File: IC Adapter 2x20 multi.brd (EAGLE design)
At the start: 74 x 56 mm, 12 parts, among them IC2 LTC6804IG-1#PBF, IC3 LTC6804IG-1#PBF, IC4 LTC6804IG-1#PBF

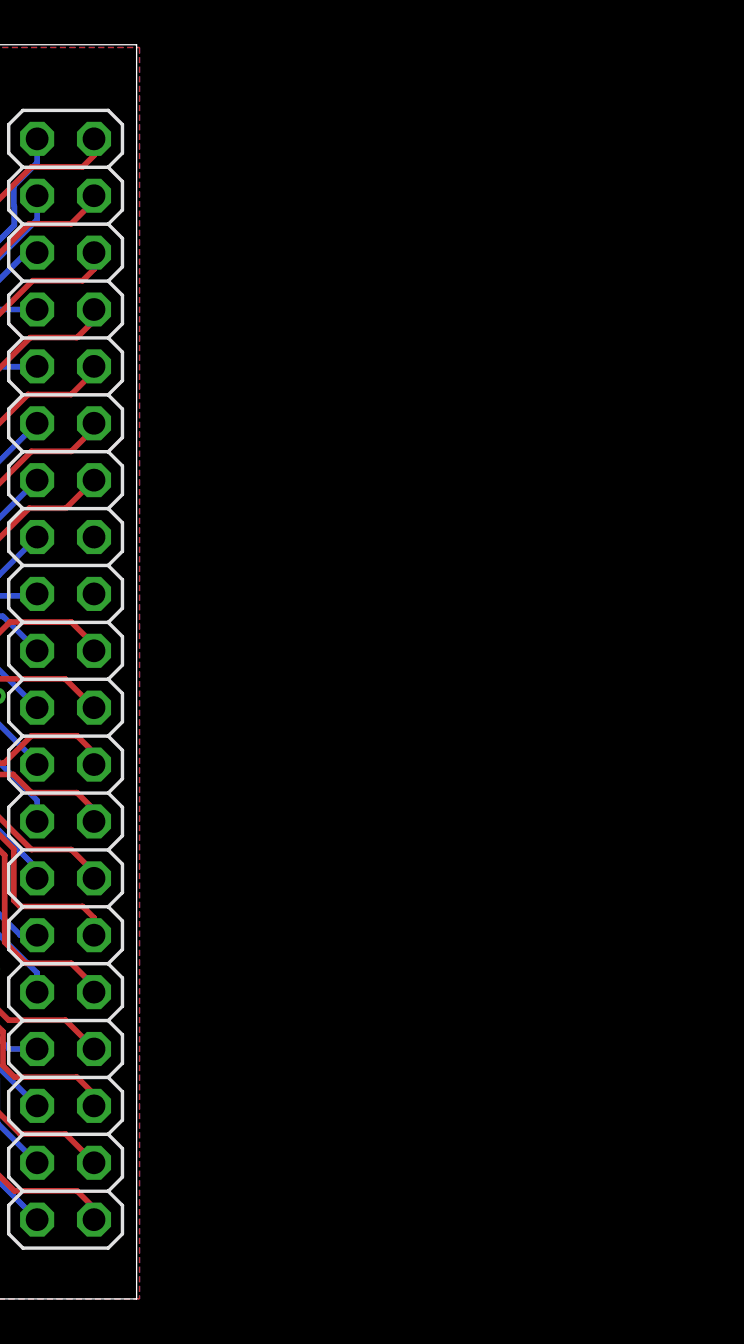
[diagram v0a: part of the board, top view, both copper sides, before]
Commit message: multi made to 4x boards
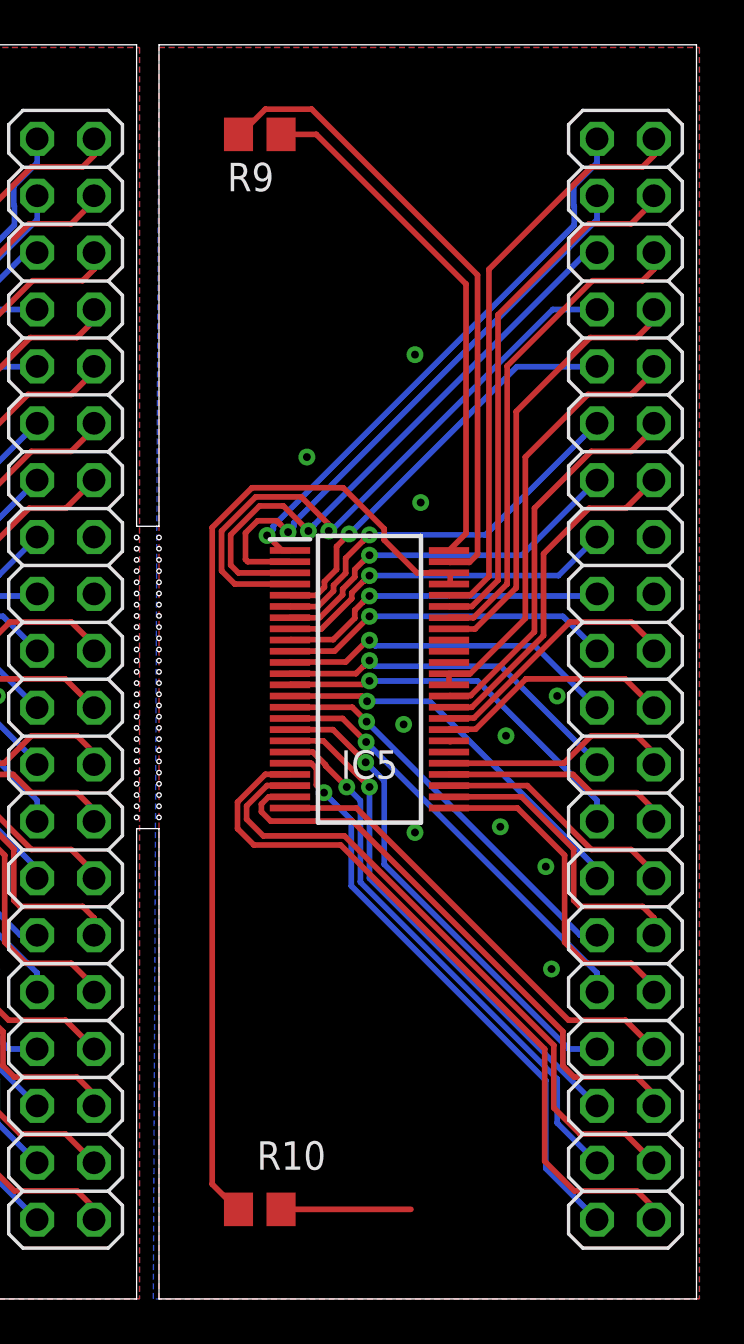
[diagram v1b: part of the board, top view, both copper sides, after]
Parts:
- added IC5: LTC6804IG-1#PBF, SamacSys_Parts:SOP50P780X200-48N
- added JP5: (no value), pinhead:2X20
- added R10: 20k, rcl:R0805
- added R9: 100R, rcl:R0805
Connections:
- new net ICMP4: IC5.45, IC5.46, R10.1
- new net N$10: IC5.47, R9.2
- new net N$9: IC5.48, R9.1
- net C0: now also IC5.26, JP5.30
- net C1: now also IC5.24, JP5.34
- net C10: now also IC5.6, JP5.11
- net C11: now also IC5.4, JP5.7
- net C12: now also IC5.2, JP5.3
- net C2: now also IC5.22, JP5.38
- net C3: now also IC5.20, JP5.39
- net C4: now also IC5.18, JP5.35
- net C5: now also IC5.16, JP5.31
- net C6: now also IC5.14, JP5.27
- net C7: now also IC5.12, JP5.23
- net C8: now also IC5.10, JP5.19
- net C9: now also IC5.8, JP5.15
- net CSB: now also IC5.41, JP5.8
- net GND: now also IC5.30, IC5.31, IC5.40, JP5.16, JP5.18, R10.2
- net GPIO1: now also IC5.27, JP5.28
- net GPIO2: now also IC5.28, JP5.26
- net GPIO3: now also IC5.29, JP5.24
- net GPIO4: now also IC5.32, JP5.22
- net GPIO5: now also IC5.33, JP5.20
- net S1: now also IC5.25, JP5.32
- net S10: now also IC5.7, JP5.13
- net S11: now also IC5.5, JP5.9
- net S12: now also IC5.3, JP5.5
- net S2: now also IC5.23, JP5.36
- net S3: now also IC5.21, JP5.40
- net S4: now also IC5.19, JP5.37
- net S5: now also IC5.17, JP5.33
- net S6: now also IC5.15, JP5.29
- net S7: now also IC5.13, JP5.25
- net S8: now also IC5.11, JP5.21
- net S9: now also IC5.9, JP5.17
- net SCK: now also IC5.42, JP5.6
- net SDI: now also IC5.43, JP5.4
- net SDO: now also IC5.44, JP5.2
- net V+: now also IC5.1, JP5.1
- net VREF1: now also IC5.35, JP5.12
- net VREF2: now also IC5.34, JP5.14
- net VREG: now also IC5.36, IC5.37, JP5.10
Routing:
- net ICMP4: track 0.00 -> 44.7 mm
- net S3: track 99.3 -> 132.4 mm
- net C2: track 87.3 -> 116.4 mm
- net N$10: track 0.00 -> 28.1 mm
- net C11: track 82.1 -> 109.5 mm, vias 3 -> 4
- net S12: track 80.0 -> 106.6 mm, vias 3 -> 4
- net C3: track 79.8 -> 106.5 mm, vias 3 -> 4
- net C12: track 78.8 -> 105.1 mm, vias 3 -> 4
- net SDO: track 78.2 -> 104.3 mm
- net S2: track 77.8 -> 103.7 mm
- net V+: track 75.4 -> 100.5 mm, vias 3 -> 4
- net S4: track 73.8 -> 98.5 mm, vias 3 -> 4
- net SDI: track 71.5 -> 95.3 mm
- net N$9: track 0.00 -> 23.2 mm
- net C4: track 68.6 -> 91.4 mm, vias 3 -> 4
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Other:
- board size 74 x 56 mm -> 99 x 56 mm
